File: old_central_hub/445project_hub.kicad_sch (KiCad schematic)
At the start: 59 parts, among them J101 Barrel_Jack_Switch, J102 USB_B, J103 USB, J104 USB, SW101 SW_Push, U101 MCP1826S, U102 SN75240, U103 TUSB2077A, U104 SN75240, U105 SN75240, Y101 6MHz

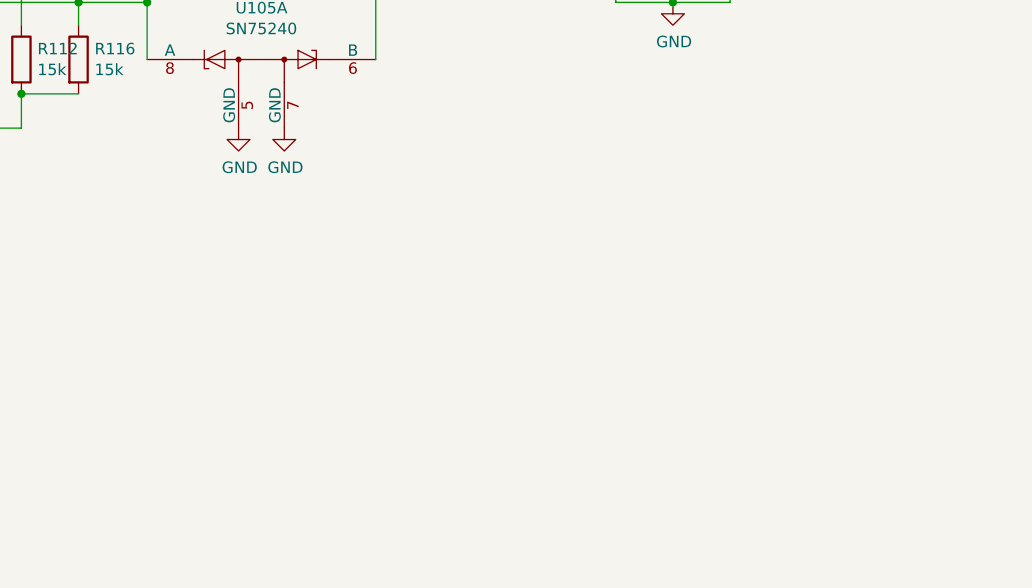
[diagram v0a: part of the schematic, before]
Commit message: Add 12V->5V converter
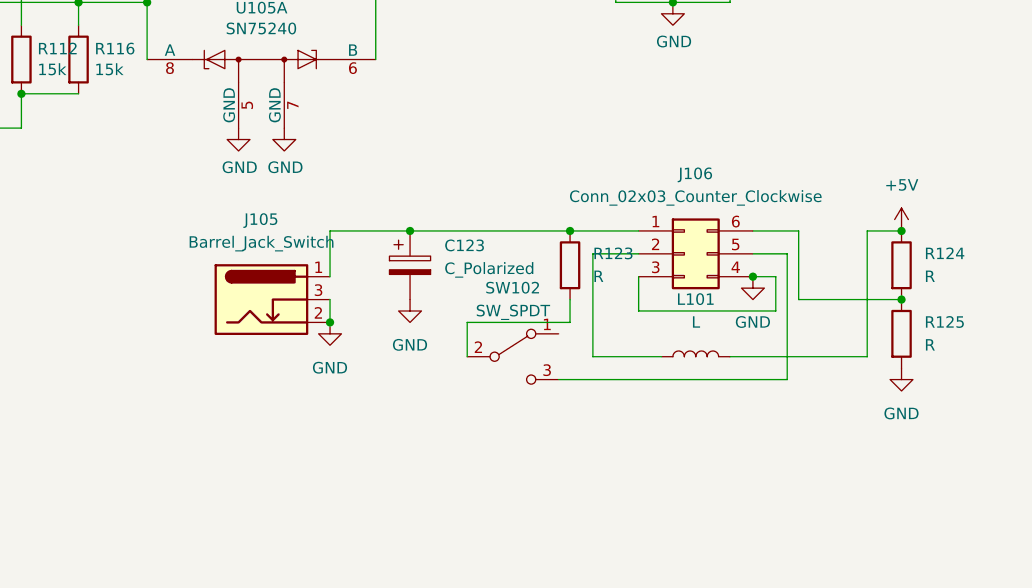
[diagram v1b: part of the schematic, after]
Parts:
- added C123: C_Polarized, Capacitor_THT:CP_Radial_D10.0mm_P5.00mm, symbol Device:C_Polarized
- added J105: Barrel_Jack_Switch, Connector_BarrelJack:BarrelJack_Horizontal, symbol Connector:Barrel_Jack_Switch
- added J106: Conn_02x03_Counter_Clockwise, Package_TO_SOT_SMD:SOT-563, symbol Connector_Generic:Conn_02x03_Counter_Clockwise
- added L101: L, Inductor_THT:L_Radial_D12.5mm_P7.00mm_Fastron_09HCP, symbol Device:L
- added R123, R124, R125: R, Resistor_SMD:R_0603_1608Metric, symbol Device:R
- added SW102: SW_SPDT, Connector_PinSocket_2.54mm:PinSocket_1x03_P2.54mm_Vertical, symbol Switch:SW_SPDT
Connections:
- net +5V: now also L101.2, R124.1
- net GND: now also C123.2, J105.2, J105.3, J106.3 (Pin_3), J106.4 (Pin_4), R125.2
- new net: J106.2 (Pin_2), L101.1
- new net: J106.6 (Pin_6), R124.2, R125.1
- new net: C123.1, J105.1, J106.1 (Pin_1), R123.1
- new net: R123.2, SW102.2 (B)
- new net: J106.5 (Pin_5), SW102.3 (C)
